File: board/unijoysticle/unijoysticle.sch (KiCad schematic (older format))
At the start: 10 parts, among them J1 DB9_Female, J2 DB9_Female, J3 Barrel_Jack, SW1 SW_SPDT, U1 4066, U2 4066, U4 4066, U5 4066

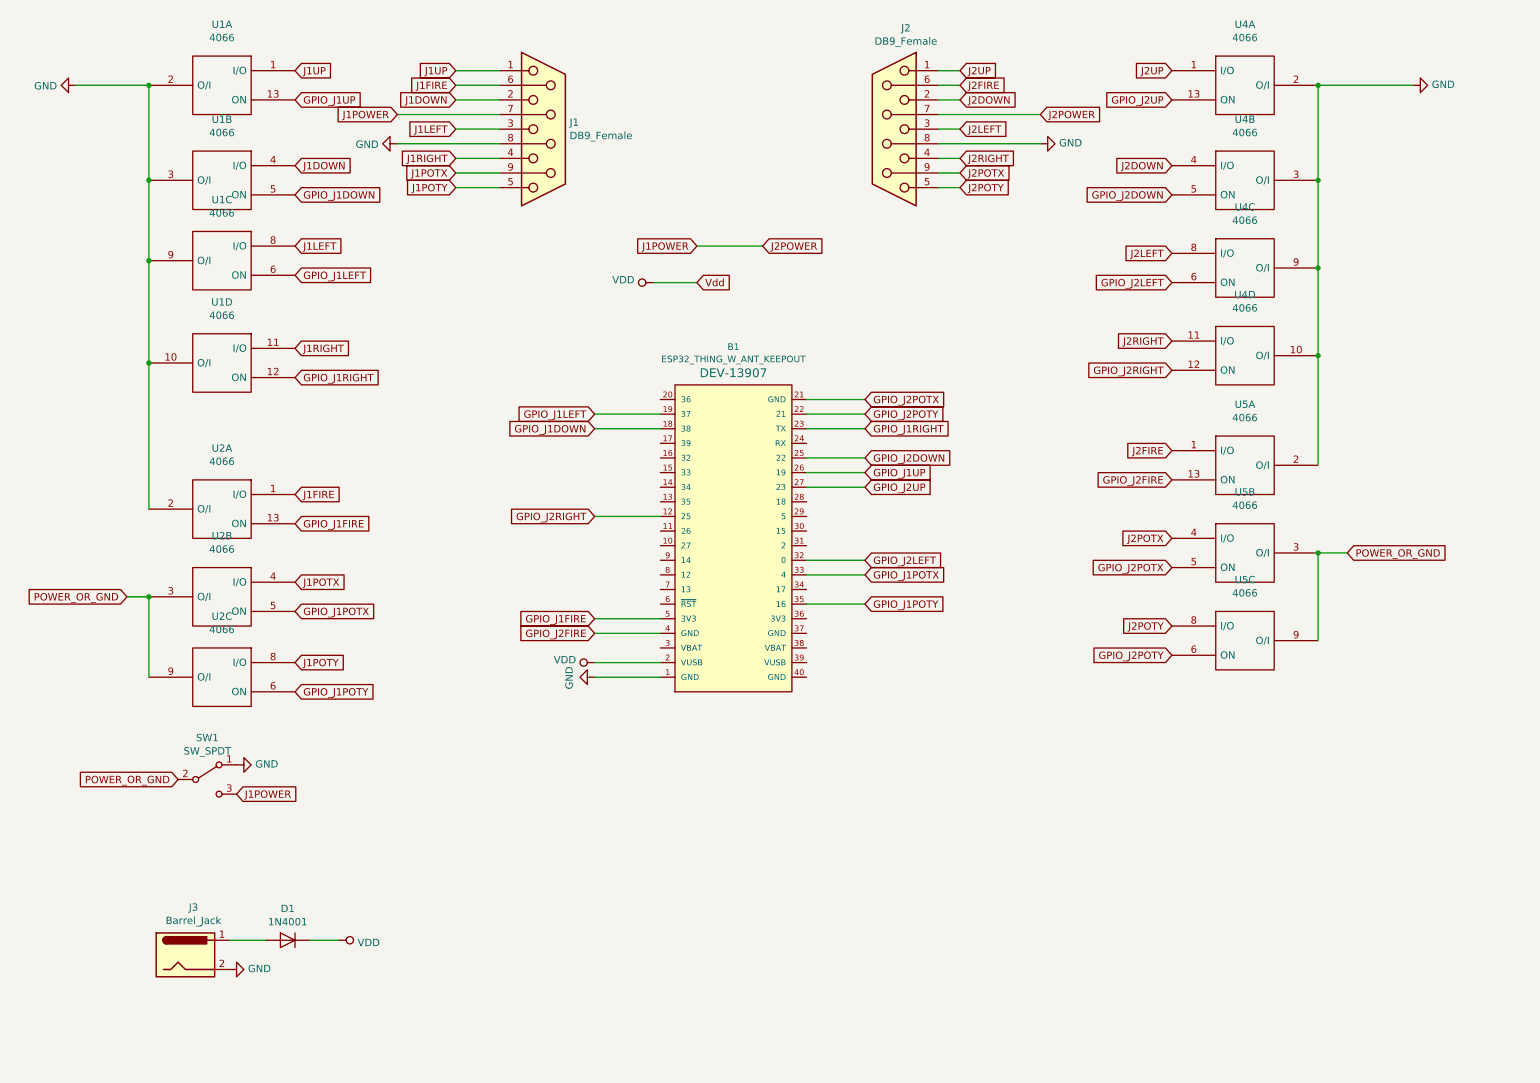
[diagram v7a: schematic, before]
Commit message: board: 4066 that controsl pots powered by c64
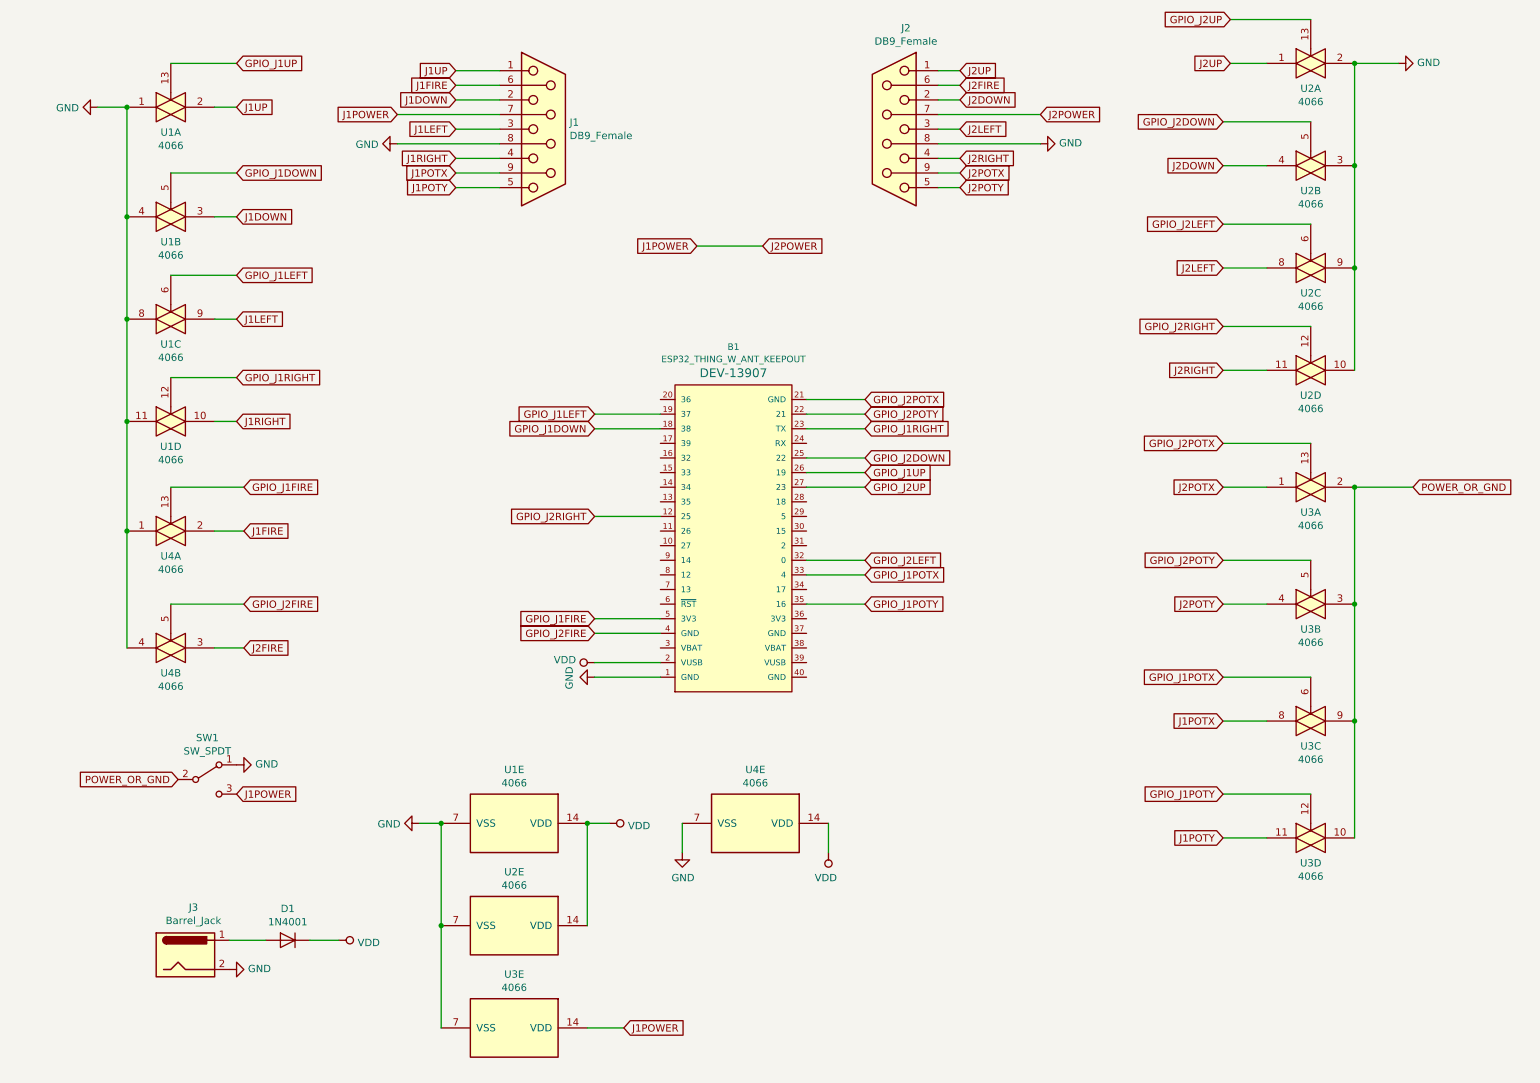
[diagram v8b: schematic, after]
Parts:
- removed U1, U2, U4, U5: 4066, symbol 4xxx_IEEE:4066
- added U1, U2, U3, U4: 4066, Package_DIP:DIP-14_W7.62mm_LongPads, symbol 4xxx:4066
- B1: footprint ESP32_THING -> Parts:MH-ET_LIVE_MINIKIT_ESP32
- J1, J2: footprint (none) -> Connector_Dsub:DSUB-9_Female_Horizontal_P2.77x2.84mm_EdgePinOffset9.40mm
- J3: footprint (none) -> Connector_BarrelJack:BarrelJack_Horizontal
- SW1: footprint (none) -> Switches:SWITCH_SPDT_PTH_11.6X4.0MM_LOCK
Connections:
- net GND: now also U1.1, U1.11, U1.4, U1.7 (VSS), U1.8, U2.10, U2.2, U2.3, U2.7 (VSS), U2.9, U3.7 (VSS), U4.1, U4.4, U4.7 (VSS)
- net GPIO_J1DOWN: now also U1.5
- net GPIO_J1FIRE: now also U4.13
- net GPIO_J1LEFT: now also U1.6
- net GPIO_J1POTX: now also U3.6
- net GPIO_J1POTY: now also U3.12
- net GPIO_J1RIGHT: now also U1.12
- net GPIO_J1UP: now also U1.13
- net GPIO_J2DOWN: now also U2.5
- net GPIO_J2FIRE: now also U4.5
- net GPIO_J2LEFT: now also U2.6
- net GPIO_J2POTX: now also U3.13
- net GPIO_J2POTY: now also U3.5
- net GPIO_J2RIGHT: now also U2.12
- net GPIO_J2UP: now also U2.13
- net J1DOWN: now also U1.3
- net J1FIRE: now also U4.2
- net J1LEFT: now also U1.9
- net J1POTX: now also U3.8
- net J1POTY: now also U3.11
- net J1POWER: now also U3.14 (VDD)
- net J1RIGHT: now also U1.10
- net J1UP: now also U1.2
- net J2DOWN: now also U2.4
- net J2FIRE: now also U4.3
- net J2LEFT: now also U2.8
- net J2POTX: now also U3.1
- net J2POTY: now also U3.4
- net J2RIGHT: now also U2.11
- net J2UP: now also U2.1
- net POWER_OR_GND: now also U3.10, U3.2, U3.3, U3.9
- net VDD: now also U1.14 (VDD), U2.14 (VDD), U4.14 (VDD)
